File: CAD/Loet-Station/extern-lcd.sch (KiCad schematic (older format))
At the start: 1 part, among them J601 IO_Conn

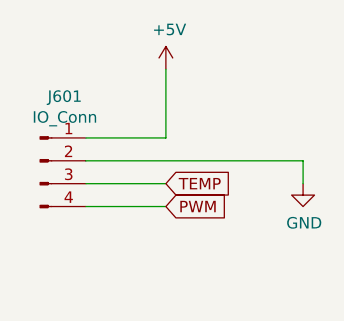
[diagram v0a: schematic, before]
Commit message: esp32-mini added, pwm driver for 24v
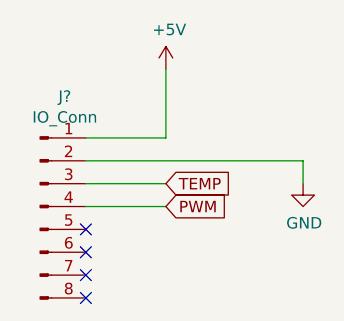
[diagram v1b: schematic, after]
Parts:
- removed J601: IO_Conn, Connector_PinHeader_2.54mm:PinHeader_1x04_P2.54mm_Vertical, symbol Connector:Conn_01x04_Male
- added J?: IO_Conn, symbol Connector:Conn_01x08_Male
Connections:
- net +5V: now also J?.1 (Pin_1)
- net GND: now also J?.2 (Pin_2)
- net PWM: now also J?.4 (Pin_4)
- net TEMP: now also J?.3 (Pin_3)
- no-connect marks 0 -> 4
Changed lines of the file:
@@
 $Descr A4 11693 8268
 encoding utf-8
-Sheet 6 6
+Sheet 7 7
 Title ""
 Date ""
@@
 Comment4 ""
 $EndDescr
-$Comp
-L Connector:Conn_01x04_Male J601
-U 1 1 603F45A4
-P 4750 2900
-F 0 "J601" H 4858 3181 50  0000 C CNN
-F 1 "IO_Conn" H 4858 3090 50  0000 C CNN
-F 2 "Connector_PinHeader_2.54mm:PinHeader_1x04_P2.54mm_Vertical" H 4750 2900 50  0001 C CNN
-F 3 "~" H 4750 2900 50  0001 C CNN
-	1    4750 2900
-	1    0    0    -1
-$EndComp
 $Comp
 L power:+5V #PWR0601
@@
 Wire Wire Line
 	4950 2800 5300 2800
+$Comp
+L Connector:Conn_01x08_Male J?
+U 1 1 603E87EA
+P 4750 3100
+F 0 "J?" H 4858 3581 50  0000 C CNN
+F 1 "IO_Conn" H 4858 3490 50  0000 C CNN
+F 2 "" H 4750 3100 50  0001 C CNN
+F 3 "~" H 4750 3100 50  0001 C CNN
+	1    4750 3100
+	1    0    0    -1
+$EndComp
+NoConn ~ 4950 3200
+NoConn ~ 4950 3300
+NoConn ~ 4950 3400
+NoConn ~ 4950 3500
 $EndSCHEMATC

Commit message: changed d1 mini pins, optional i2c oled
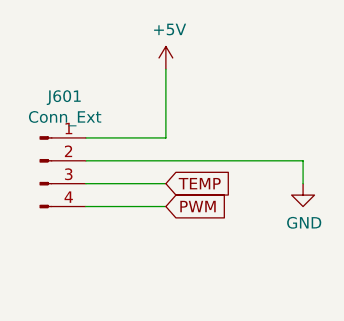
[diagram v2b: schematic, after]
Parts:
- removed J?: IO_Conn, symbol Connector:Conn_01x08_Male
- added J601: Conn_Ext, Connector_PinHeader_2.54mm:PinHeader_1x04_P2.54mm_Vertical, symbol Connector:Conn_01x04_Male
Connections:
- net +5V: now also J601.1 (Pin_1)
- net GND: now also J601.2 (Pin_2)
- net PWM: now also J601.4 (Pin_4)
- net TEMP: now also J601.3 (Pin_3)
- no-connect marks 4 -> 0
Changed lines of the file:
@@
 $Descr A4 11693 8268
 encoding utf-8
-Sheet 7 7
+Sheet 6 6
 Title ""
 Date ""
@@
 	4950 2800 5300 2800
 $Comp
-L Connector:Conn_01x08_Male J?
-U 1 1 603E87EA
-P 4750 3100
-F 0 "J?" H 4858 3581 50  0000 C CNN
-F 1 "IO_Conn" H 4858 3490 50  0000 C CNN
-F 2 "" H 4750 3100 50  0001 C CNN
-F 3 "~" H 4750 3100 50  0001 C CNN
-	1    4750 3100
+L Connector:Conn_01x04_Male J601
+U 1 1 6050DE23
+P 4750 2900
+F 0 "J601" H 4858 3181 50  0000 C CNN
+F 1 "Conn_Ext" H 4858 3090 50  0000 C CNN
+F 2 "Connector_PinHeader_2.54mm:PinHeader_1x04_P2.54mm_Vertical" H 4750 2900 50  0001 C CNN
+F 3 "~" H 4750 2900 50  0001 C CNN
+	1    4750 2900
 	1    0    0    -1
 $EndComp
-NoConn ~ 4950 3200
-NoConn ~ 4950 3300
-NoConn ~ 4950 3400
-NoConn ~ 4950 3500
 $EndSCHEMATC
